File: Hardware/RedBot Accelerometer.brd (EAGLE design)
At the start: 11.4 x 17.8 mm, 17 parts, among them U1 MMA8452Q, U2 MIC5205-3.3V, U3 PCA9306

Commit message: Rev for v11 protos
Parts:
- added JP2: (no value), SparkFun-Connectors:2X3_SMD
- C1, C2, C3, C4: device SparkFun-Capacitors:0402-CAP -> SparkFun-Capacitors:0603-CAP
- JP1: device SparkFun-Connectors:2X3-NS -> SparkFun-Connectors:2X3_SMT_POSTS
- R1, R2, R3, R4, R5, R6: device SparkFun-Resistors:0402-RES -> SparkFun-Resistors:0603-RES
- moved FRAME1 78.7 mm to (0.00, -12.7)
- moved LOGO1 8.81 mm to (0.51, 10.0)
- moved C1 3.17 mm to (12.1, 9.53)
- moved C2 3.17 mm to (12.1, 8.26)
- moved U2 3.17 mm to (12.1, 5.08)
- moved R6 2.77 mm to (7.18, 13.1)
- moved R5 2.54 mm to (6.35, 9.40)
- moved C4 2.54 mm to (3.17, 12.7)
- moved JP1 2.54 mm to (5.08, 3.81)
- moved U3 2.54 mm to (5.08, 12.7)
- moved LOGO2 2.54 mm to (11.4, 14.2)
- moved U1 2.54 mm to (11.4, 12.7)
- moved R1 2.32 mm to (8.64, 11.8)
- moved C3 1.78 mm to (10.9, 15.9), turned to 180 degrees
- moved R4 1.28 mm to (2.54, 9.40)
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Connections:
- net 5V: now also JP2.3, JP2.4
- net GND: now also JP2.5, JP2.6
- net SCL: now also JP2.1
- net SDA: now also JP2.2
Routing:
- net 3.3V: track 32.9 -> 47.8 mm, vias 2 -> 4
- net 5V: track 26.9 -> 38.7 mm, vias 0 -> 3
- net SDA1: track 12.1 -> 18.7 mm
- net GND: track 8.60 -> 2.66 mm
- net SDA: track 6.46 -> 9.07 mm, vias 0 -> 1
- net SCL: track 7.46 -> 8.58 mm, vias 0 -> 1
- net N$2: track 6.19 -> 7.19 mm
- net N$1: track 1.35 -> 2.17 mm
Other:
- board size 11.4 x 17.8 mm -> 14 x 17.8 mm
- board text added: "v11"
- board text removed: "v10"

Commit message: added fiducials to board
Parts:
- added FID1, FID2: FIDUCIALUFIDUCIAL, SparkFun-Aesthetics:MICRO-FIDUCIAL
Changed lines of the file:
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@@
 <?xml version="1.0" encoding="utf-8"?>
 <!DOCTYPE eagle SYSTEM "eagle.dtd">
-<eagle version="6.4">
+<eagle version="6.5.0">
 <drawing>
 <settings>
@@
 <setting verticaltext="up"/>
 </settings>
-<grid distance="0.05" unitdist="inch" unit="inch" style="lines" multiple="1" display="yes" altdistance="0.005" altunitdist="inch" altunit="inch"/>
+<grid distance="0.01" unitdist="inch" unit="inch" style="lines" multiple="1" display="yes" altdistance="0.001" altunitdist="inch" altunit="inch"/>
 <layers>
 <layer number="1" name="Top" color="4" fill="1" visible="yes" active="yes"/>
-<layer number="2" name="Route2" color="1" fill="3" visible="no" active="yes"/>
-<layer number="15" name="Route15" color="4" fill="6" visible="no" active="yes"/>
+<layer number="2" name="Route2" color="1" fill="3" visible="yes" active="yes"/>
+<layer number="15" name="Route15" color="4" fill="6" visible="yes" active="yes"/>
 <layer number="16" name="Bottom" color="1" fill="1" visible="yes" active="yes"/>
 <layer number="17" name="Pads" color="2" fill="1" visible="yes" active="yes"/>
 <layer number="18" name="Vias" color="2" fill="1" visible="yes" active="yes"/>
 <layer number="19" name="Unrouted" color="6" fill="1" visible="yes" active="yes"/>
-<layer number="20" name="Dimension" color="15" fill="1" visible="yes" active="yes"/>
-<layer number="21" name="tPlace" color="16" fill="1" visible="yes" active="yes"/>
-<layer number="22" name="bPlace" color="14" fill="1" visible="yes" active="yes"/>
+<layer number="20" name="Dimension" color="6" fill="1" visible="yes" active="yes"/>
+<layer number="21" name="tPlace" color="6" fill="1" visible="yes" active="yes"/>
+<layer number="22" name="bPlace" color="6" fill="1" visible="yes" active="yes"/>
 <layer number="23" name="tOrigins" color="15" fill="1" visible="yes" active="yes"/>
 <layer number="24" name="bOrigins" color="15" fill="1" visible="yes" active="yes"/>
-<layer number="25" name="tNames" color="7" fill="1" visible="no" active="yes"/>
-<layer number="26" name="bNames" color="7" fill="1" visible="no" active="yes"/>
-<layer number="27" name="tValues" color="7" fill="1" visible="no" active="yes"/>
-<layer number="28" name="bValues" color="7" fill="1" visible="no" active="yes"/>
-<layer number="29" name="tStop" color="7" fill="3" visible="no" active="yes"/>
-<layer number="30" name="bStop" color="7" fill="6" visible="no" active="yes"/>
-<layer number="31" name="tCream" color="7" fill="4" visible="no" active="yes"/>
-<layer number="32" name="bCream" color="7" fill="5" visible="no" active="yes"/>
-<layer number="39" name="tKeepout" color="4" fill="11" visible="no" active="yes"/>
-<layer number="40" name="bKeepout" color="1" fill="11" visible="no" active="yes"/>
-<layer number="41" name="tRestrict" color="4" fill="10" visible="no" active="yes"/>
-<layer number="42" name="bRestrict" color="1" fill="10" visible="no" active="yes"/>
-<layer number="43" name="vRestrict" color="2" fill="10" visible="no" active="yes"/>
-<layer number="44" name="Drills" color="7" fill="1" visible="no" active="yes"/>
+<layer number="25" name="tNames" color="7" fill="1" visible="yes" active="yes"/>
+<layer number="26" name="bNames" color="7" fill="1" visible="yes" active="yes"/>
+<layer number="27" name="tValues" color="7" fill="1" visible="yes" active="yes"/>
+<layer number="28" name="bValues" color="7" fill="1" visible="yes" active="yes"/>
+<layer number="29" name="tStop" color="7" fill="3" visible="yes" active="yes"/>
+<layer number="30" name="bStop" color="7" fill="6" visible="yes" active="yes"/>
+<layer number="31" name="tCream" color="7" fill="4" visible="yes" active="yes"/>
+<layer number="32" name="bCream" color="7" fill="5" visible="yes" active="yes"/>
+<layer number="39" name="tKeepout" color="4" fill="11" visible="yes" active="yes"/>
+<layer number="40" name="bKeepout" color="1" fill="11" visible="yes" active="yes"/>
+<layer number="41" name="tRestrict" color="4" fill="10" visible="yes" active="yes"/>
+<layer number="42" name="bRestrict" color="1" fill="10" visible="yes" active="yes"/>
+<layer number="43" name="vRestrict" color="2" fill="10" visible="yes" active="yes"/>
+<layer number="44" name="Drills" color="7" fill="1" visible="yes" active="yes"/>
 <layer number="45" name="Holes" color="7" fill="1" visible="yes" active="yes"/>
-<layer number="46" name="Milling" color="3" fill="1" visible="no" active="yes"/>
+<layer number="46" name="Milling" color="3" fill="1" visible="yes" active="yes"/>
 <layer number="51" name="tDocu" color="6" fill="1" visible="yes" active="yes"/>
-<layer number="52" name="bDocu" color="7" fill="1" visible="no" active="yes"/>
+<layer number="52" name="bDocu" color="7" fill="1" visible="yes" active="yes"/>
 <layer number="3" name="Route3" color="4" fill="3" visible="no" active="no"/>
 <layer number="4" name="Route4" color="1" fill="4" visible="no" active="no"/>
@@
 <attribute name="PROD_ID" value="CONN-11290" x="5.08" y="3.81" size="1.778" layer="28" font="vector" ratio="15" rot="MR270" display="off"/>
 </element>
+<element name="FID1" library="SparkFun-Aesthetics" package="MICRO-FIDUCIAL" value="FIDUCIALUFIDUCIAL" x="13.208" y="0.762"/>
+<element name="FID2" library="SparkFun-Aesthetics" package="MICRO-FIDUCIAL" value="FIDUCIALUFIDUCIAL" x="5.588" y="17.018"/>
 </elements>
 <signals>

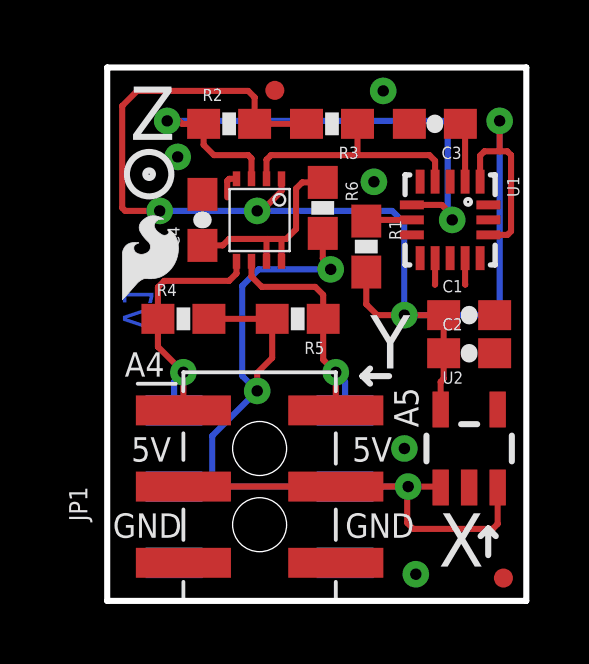
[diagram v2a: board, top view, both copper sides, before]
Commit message: Added 1:1 for PCA and Accel , 0603 update
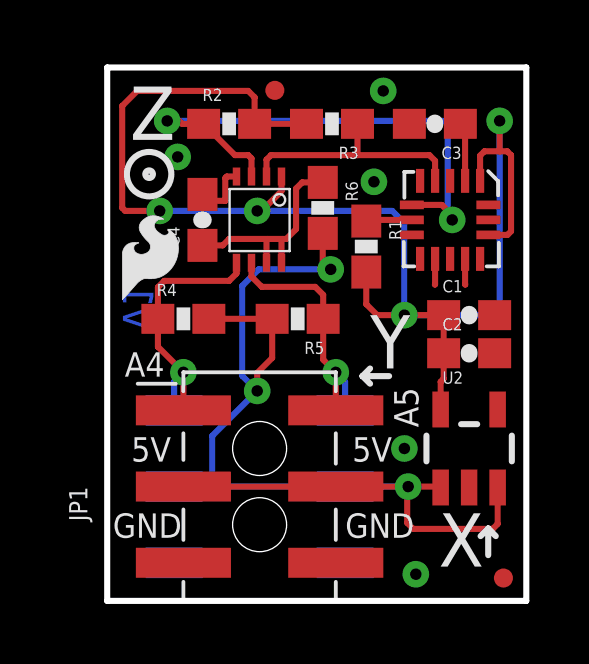
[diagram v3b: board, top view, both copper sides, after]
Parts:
- U1: value MMA8452Q -> MMA8452QMMA8452Q-1:1; device SparkFun-Sensors:QFN-16_0.5MM -> SparkFun-Sensors:MMA8452Q-1:1
- U3: device SparkFun-DigitalIC:PSOP-8 -> SparkFun-DigitalIC:PCA9306DC-1:1
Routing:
- net GND: track 2.66 -> 3.73 mm
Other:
- board text added: "Revised by: Patrick Alberts"

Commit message: Fixing version numbers
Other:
- board text added: "v12"
- board text removed: "v11"
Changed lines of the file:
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@@
 <?xml version="1.0" encoding="utf-8"?>
 <!DOCTYPE eagle SYSTEM "eagle.dtd">
-<eagle version="6.4">
+<eagle version="6.6.0">
 <drawing>
 <settings>
@@
 <layer number="108" name="tplace-old" color="10" fill="1" visible="no" active="no"/>
 <layer number="109" name="ref-old" color="11" fill="1" visible="no" active="no"/>
-<layer number="110" name="fp0" color="7" fill="1" visible="yes" active="yes"/>
-<layer number="111" name="LPC17xx" color="7" fill="1" visible="yes" active="yes"/>
-<layer number="112" name="tSilk" color="7" fill="1" visible="yes" active="yes"/>
-<layer number="113" name="IDFDebug" color="7" fill="1" visible="yes" active="yes"/>
+<layer number="110" name="fp0" color="7" fill="1" visible="no" active="yes"/>
+<layer number="111" name="LPC17xx" color="7" fill="1" visible="no" active="yes"/>
+<layer number="112" name="tSilk" color="7" fill="1" visible="no" active="yes"/>
+<layer number="113" name="IDFDebug" color="7" fill="1" visible="no" active="yes"/>
 <layer number="116" name="Patch_BOT" color="9" fill="4" visible="no" active="no"/>
 <layer number="121" name="_tsilk" color="7" fill="1" visible="no" active="no"/>
 <layer number="122" name="_bsilk" color="7" fill="1" visible="no" active="no"/>
-<layer number="123" name="tTestmark" color="7" fill="1" visible="yes" active="yes"/>
-<layer number="124" name="bTestmark" color="7" fill="1" visible="yes" active="yes"/>
+<layer number="123" name="tTestmark" color="7" fill="1" visible="no" active="yes"/>
+<layer number="124" name="bTestmark" color="7" fill="1" visible="no" active="yes"/>
 <layer number="125" name="_tNames" color="7" fill="1" visible="no" active="no"/>
-<layer number="126" name="_bNames" color="7" fill="1" visible="yes" active="yes"/>
-<layer number="127" name="_tValues" color="7" fill="1" visible="yes" active="yes"/>
-<layer number="128" name="_bValues" color="7" fill="1" visible="yes" active="yes"/>
-<layer number="131" name="tAdjust" color="7" fill="1" visible="yes" active="yes"/>
-<layer number="132" name="bAdjust" color="7" fill="1" visible="yes" active="yes"/>
+<layer number="126" name="_bNames" color="7" fill="1" visible="no" active="yes"/>
+<layer number="127" name="_tValues" color="7" fill="1" visible="no" active="yes"/>
+<layer number="128" name="_bValues" color="7" fill="1" visible="no" active="yes"/>
+<layer number="131" name="tAdjust" color="7" fill="1" visible="no" active="yes"/>
+<layer number="132" name="bAdjust" color="7" fill="1" visible="no" active="yes"/>
 <layer number="144" name="Drill_legend" color="7" fill="1" visible="no" active="no"/>
-<layer number="150" name="Notes" color="7" fill="1" visible="yes" active="yes"/>
+<layer number="150" name="Notes" color="7" fill="1" visible="no" active="yes"/>
 <layer number="151" name="HeatSink" color="7" fill="1" visible="no" active="no"/>
-<layer number="152" name="_bDocu" color="7" fill="1" visible="yes" active="yes"/>
-<layer number="153" name="FabDoc1" color="7" fill="1" visible="yes" active="yes"/>
-<layer number="154" name="FabDoc2" color="7" fill="1" visible="yes" active="yes"/>
-<layer number="155" name="FabDoc3" color="7" fill="1" visible="yes" active="yes"/>
+<layer number="152" name="_bDocu" color="7" fill="1" visible="no" active="yes"/>
+<layer number="153" name="FabDoc1" color="7" fill="1" visible="no" active="yes"/>
+<layer number="154" name="FabDoc2" color="7" fill="1" visible="no" active="yes"/>
+<layer number="155" name="FabDoc3" color="7" fill="1" visible="no" active="yes"/>
 <layer number="199" name="Contour" color="7" fill="1" visible="no" active="no"/>
 <layer number="200" name="200bmp" color="1" fill="10" visible="no" active="no"/>
@@
 <layer number="223" name="223bmp" color="24" fill="1" visible="no" active="no"/>
 <layer number="224" name="224bmp" color="25" fill="1" visible="no" active="no"/>
-<layer number="248" name="Housing" color="7" fill="1" visible="yes" active="yes"/>
-<layer number="249" name="Edge" color="7" fill="1" visible="yes" active="yes"/>
+<layer number="248" name="Housing" color="7" fill="1" visible="no" active="yes"/>
+<layer number="249" name="Edge" color="7" fill="1" visible="no" active="yes"/>
 <layer number="250" name="Descript" color="3" fill="1" visible="no" active="no"/>
 <layer number="251" name="SMDround" color="12" fill="11" visible="no" active="no"/>
@@
 <text x="6.35" y="7.62" size="0.8128" layer="22" font="vector" ratio="15" rot="MR270" align="center-right">SCL</text>
 <text x="3.81" y="7.62" size="0.8128" layer="22" font="vector" ratio="15" rot="MR270" align="center-right">SDA</text>
-<text x="1.541" y="11.386" size="1.016" layer="16" font="vector" ratio="15" rot="MR270">v11</text>
+<text x="1.541" y="11.386" size="1.016" layer="16" font="vector" ratio="15" rot="MR270">v12</text>
 <text x="31.75" y="-12.7" size="1.778" layer="51" font="vector" ratio="15">M. Hord</text>
 <text x="1.247" y="7.474" size="0.8128" layer="21" font="vector" ratio="15" align="bottom-center">A4</text>
